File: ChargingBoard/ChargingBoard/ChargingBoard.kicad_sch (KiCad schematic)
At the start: 142 parts, among them J1 Conn_02x03_Odd_Even, J17 Micro_SD_Card, J2 Screw_Terminal_01x02, J3 Screw_Terminal_01x02, J4 Screw_Terminal_01x02, J5 Screw_Terminal_01x02, Q1 FQP27P06, Q10 FQP27P06, Q11 FQP27P06, Q12 IRLZ44N, Q13 FQP27P06, Q14 FQP27P06, Q15 FQP27P06, Q16 IRLZ44N, Q2 FQP27P06, Q3 FQP27P06, Q4 IRLZ44N, Q5 FQP27P06, Q6 FQP27P06, Q7 FQP27P06, Q8 IRLZ44N, Q9 FQP27P06, U1 LTC4011CFE, U2 LTC4011CFE, U3 LP2985-3.3, U4 LTC4011CFE, U5 LTC4011CFE, U6 ATmega328P-A, U9 CD4050BPWR, Y1 16MHz

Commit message: Voltage Sensors Added
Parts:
- added C24: 0.1u, Capacitor_SMD:C_0603_1608Metric_Pad1.08x0.95mm_HandSolder, symbol Device:C
- added U7, U8: INA260, Package_SO:TSSOP-16_4.4x5mm_P0.65mm, symbol Sensor:INA260
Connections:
- net +5V: now also U7.10 (VS), U7.5 (A0), U8.10 (VS)
- net GND: now also C24.2, U7.11 (GND), U7.4 (A1), U7.6 (GND), U8.11 (GND), U8.4 (A1), U8.5 (A0), U8.6 (GND)
- net SD_CS: now also U6.14 (PB2); no longer U6.27 (PC4)
- net at U6.20 (AREF): now also C24.1
- net SCL: now reaches U6.28 (PC5)
- net SCL: now also U7.9 (SCL), U8.9 (SCL)
- new net: U7.1 (IN+), U7.12 (VBUS), U7.2 (IN+), U7.3 (IN+)
- new net: U8.1 (IN+), U8.12 (VBUS), U8.2 (IN+), U8.3 (IN+)
- new net Motor_Load: U8.14 (IN-), U8.15 (IN-), U8.16 (IN-)
- new net PCB_Load: U7.14 (IN-), U7.15 (IN-), U7.16 (IN-)
- new net SDA: U6.27 (PC4), U7.8 (SDA), U8.8 (SDA)
- no-connect marks 5 -> 21
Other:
- note added: "Motor Battery V/A Sensor"
- note added: "PCB Battery V/A Sensor"

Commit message: Fixed Power Flags
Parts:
- added J6: Conn_01x03_Pin, symbol Connector:Conn_01x03_Pin
- added J7: Screw_Terminal_01x02, symbol Connector:Screw_Terminal_01x02
- U3: footprint Package_TO_SOT_SMD:SOT-23-5_HandSoldering -> Package_TO_SOT_SMD:SOT-23-5
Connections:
- net DCIN1 is gone; now on net +34V_DCIN: J2.1 (Pin_1), J3.1 (Pin_1)
- net DCIN2 is gone; now on net +18V_DCIN: J4.1 (Pin_1)
- net BAT1: no longer R48.1, U5.12 (BAT)
- net BAT4: now also R48.1, U5.12 (BAT)
- net GND: now also J6.1 (Pin_1), J7.2 (Pin_2)
- net RX: now also J6.3 (Pin_3)
- net TX: now also J6.2 (Pin_2)
- net +18V_VCC: now reaches U7.1 (IN+), U7.12 (VBUS), U7.2 (IN+), U7.3 (IN+)
- net +18V_VCC: now also C15.1, C20.1, D15.1 (K), D20.1 (K), Q10.3 (S), Q11.3 (S), Q13.3 (S), Q14.3 (S), Q15.3 (S), Q9.3 (S), U4.18 (V_{CC}), U5.18 (V_{CC})
- net at J17.3 (CMD), U9.4: no longer J17.5 (CLK), U9.2
- net +12V renamed +34V_VCC
- net +34V_VCC: now also C10.1, C5.1, D10.1 (K), D5.1 (K), Q1.3 (S), Q2.3 (S), Q3.3 (S), Q6.3 (S), Q7.3 (S), U1.18 (V_{CC}), U2.18 (V_{CC}); no longer Q13.3 (S)
- net +18V renamed +18V_DCIN
- net +18V_DCIN: now also J7.1 (Pin_1); no longer C15.1, C20.1, D15.1 (K), D20.1 (K), Q10.3 (S), Q11.3 (S), Q14.3 (S), Q15.3 (S), Q9.3 (S), U4.18 (V_{CC}), U5.18 (V_{CC})
- net +34V renamed +34V_DCIN
- net +34V_DCIN: no longer C10.1, C5.1, D10.1 (K), D5.1 (K), Q1.3 (S), Q2.3 (S), Q3.3 (S), Q6.3 (S), Q7.3 (S), U1.18 (V_{CC}), U2.18 (V_{CC})
- new net: J17.5 (CLK), U9.2
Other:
- moved on the sheet: C22, C23, J5, U3, U7, U8

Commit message: Component Reworks
Changed MOSFET component footprints, diodes, etc.
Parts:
- removed C14, C19, C4, C9: 10u, Capacitor_SMD:C_0201_0603Metric_Pad0.64x0.40mm_HandSolder, symbol Device:C
- removed Q10, Q11, Q13, Q14, Q15, Q9: FQP27P06, Package_TO_SOT_THT:TO-220-3_Vertical, symbol Transistor_FET:FQP27P06
- added C14, C19, C4, C9: 10u, Capacitor_THT:CP_Radial_D5.0mm_P2.00mm, symbol Device:C_Polarized
- added Q10, Q9: FDC658AP, Package_TO_SOT_SMD:SuperSOT-6, symbol FDC658AP:FDC658AP
- added U10, U11: FDS6975, Package_SO:SOIC-8_3.9x4.9mm_P1.27mm, symbol FDS6975:FDS6975
- BT1, BT2, BT3, BT4: footprint Battery:BatteryHolder_Keystone_1060_1x2032 -> TerminalBlock_Phoenix:TerminalBlock_Phoenix_MKDS-1,5-2-5.08_1x02_P5.08mm_Horizontal
- C1, C11, C12, C13, C16, C17, C18, C2, C3, C6, C7, C8: footprint Capacitor_SMD:C_0201_0603Metric_Pad0.64x0.40mm_HandSolder -> Capacitor_SMD:C_0603_1608Metric_Pad1.08x0.95mm_HandSolder
- C10, C15, C20, C5: footprint (none) -> Capacitor_THT:CP_Radial_D5.0mm_P2.00mm
- D1, D11, D12, D13, D14, D16, D17, D18, D19, D2, D3, D4, D6, D7, D8, D9: footprint LED_SMD:LED_0201_0603Metric_Pad0.64x0.40mm_HandSolder -> LED_SMD:LED_0603_1608Metric_Pad1.05x0.95mm_HandSolder
- D10, D15, D20, D5: footprint Diode_THT:D_DO-41_SOD81_P10.16mm_Horizontal -> Diode_SMD:D_SMA-SMB_Universal_Handsoldering
- J1: footprint (none) -> Connector_PinSocket_2.54mm:PinSocket_2x03_P2.54mm_Vertical
- J2, J3, J4, J5, J7: footprint (none) -> TerminalBlock_Phoenix:TerminalBlock_Phoenix_MKDS-1,5-2-5.08_1x02_P5.08mm_Horizontal
- J6: footprint (none) -> Connector_PinHeader_2.54mm:PinHeader_1x03_P2.54mm_Vertical
- L1, L2, L3, L4: value 6.8u -> 10u; footprint Inductor_SMD:L_0201_0603Metric_Pad0.64x0.40mm_HandSolder -> Inductor_SMD:L_0603_1608Metric_Pad1.05x0.95mm_HandSolder
- Q1, Q12, Q16, Q2, Q3, Q4, Q5, Q6, Q7, Q8: footprint Package_TO_SOT_THT:TO-220-3_Vertical -> Package_TO_SOT_SMD:TO-252-2
- R1, R10, R11, R12, R13, R14, R15, R16, R17, R18, R19, R2, R20, R21, R22, R23, R24, R25, R26, R27, R28, R29, R3, R30, R31, R32, R33, R34, R35, R36, R37, R38, R39, R4, R40, R41, R42, R43, R44, R45, R46, R47, R48, R49, R5, R50, R51, R52, R6, R7, R8, R9: footprint Resistor_SMD:R_0201_0603Metric_Pad0.64x0.40mm_HandSolder -> Resistor_SMD:R_0603_1608Metric_Pad0.98x0.95mm_HandSolder
- R54, R55, R56: footprint (none) -> Resistor_SMD:R_0603_1608Metric_Pad0.98x0.95mm_HandSolder
- TH1, TH2, TH3, TH4: footprint Resistor_SMD:R_0508_1220Metric_Pad1.12x2.15mm_HandSolder -> Resistor_SMD:R_0603_1608Metric_Pad0.98x0.95mm_HandSolder
- Y1: footprint (none) -> Crystal:Resonator_Murata_DSN6-3Pin_W7.0mm_H2.5mm
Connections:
- net +18V_DCIN: now also U10.5 (D2), U10.6 (D2), U11.5 (D2), U11.6 (D2)
- net +18V_VCC: now also Q10.4 (S), Q9.4 (S), U10.1 (S1), U10.3 (S2), U11.1 (S1), U11.3 (S2)
- net +34V_VCC: now also U8.1 (IN+), U8.12 (VBUS), U8.2 (IN+), U8.3 (IN+)
- net BAT1: now also C4.1
- net BAT2: now also C9.1
- net BAT3: now also C14.1, U10.7 (D1), U10.8 (D1)
- net BAT4: now also C19.1, U11.7 (D1), U11.8 (D1)
- net GND: now also C14.2, C19.2, C4.2, C9.2
- net INFET3: now also U10.4 (G2)
- net INFET4: now also U11.4 (G2)
- net L3: now also Q10.1 (D), Q10.2 (D), Q10.5 (D), Q10.6 (D)
- net L4: now also Q9.1 (D), Q9.2 (D), Q9.5 (D), Q9.6 (D)
- net TGATE3: now also Q10.3 (G)
- net TGATE4: now also Q9.3 (G)
- net at D20.2 (A), R47.1: now also U11.2 (G1)
- net at D15.2 (A), R34.1: now also U10.2 (G1)
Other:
- moved on the sheet: C15, C20, C24, D15, D20, J1, Q12, Q16, R21, R34, R47

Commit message: Arrangement Begins
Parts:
- BT1, BT2, BT3, BT4: footprint TerminalBlock_Phoenix:TerminalBlock_Phoenix_MKDS-1,5-2-5.08_1x02_P5.08mm_Horizontal -> TerminalBlock_Phoenix:TerminalBlock_Phoenix_MPT-0,5-2-2.54_1x02_P2.54mm_Horizontal
- D10, D5: footprint Diode_SMD:D_SMA-SMB_Universal_Handsoldering -> Diode_SMD:D_SMA_Handsoldering
- D15, D20: footprint Diode_SMD:D_SMA-SMB_Universal_Handsoldering -> Diode_SMD:D_SOD-323_HandSoldering
- J2, J3, J4, J5, J7: footprint TerminalBlock_Phoenix:TerminalBlock_Phoenix_MKDS-1,5-2-5.08_1x02_P5.08mm_Horizontal -> TerminalBlock_Phoenix:TerminalBlock_Phoenix_MKDS-1-2-3.81_1x02_P3.81mm_Horizontal
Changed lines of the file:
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@@
 			)
 		)
-		(property "Footprint" "TerminalBlock_Phoenix:TerminalBlock_Phoenix_MKDS-1,5-2-5.08_1x02_P5.08mm_Horizontal"
+		(property "Footprint" "TerminalBlock_Phoenix:TerminalBlock_Phoenix_MPT-0,5-2-2.54_1x02_P2.54mm_Horizontal"
 			(at 525.78 168.656 90)
 			(effects
@@
 			)
 		)
-		(property "Footprint" "TerminalBlock_Phoenix:TerminalBlock_Phoenix_MKDS-1,5-2-5.08_1x02_P5.08mm_Horizontal"
+		(property "Footprint" "TerminalBlock_Phoenix:TerminalBlock_Phoenix_MKDS-1-2-3.81_1x02_P3.81mm_Horizontal"
 			(at 196.85 21.59 0)
 			(effects
@@
 			)
 		)
-		(property "Footprint" "TerminalBlock_Phoenix:TerminalBlock_Phoenix_MKDS-1,5-2-5.08_1x02_P5.08mm_Horizontal"
+		(property "Footprint" "TerminalBlock_Phoenix:TerminalBlock_Phoenix_MKDS-1-2-3.81_1x02_P3.81mm_Horizontal"
 			(at 196.85 59.69 0)
 			(effects
@@
 			)
 		)
-		(property "Footprint" "TerminalBlock_Phoenix:TerminalBlock_Phoenix_MKDS-1,5-2-5.08_1x02_P5.08mm_Horizontal"
+		(property "Footprint" "TerminalBlock_Phoenix:TerminalBlock_Phoenix_MKDS-1-2-3.81_1x02_P3.81mm_Horizontal"
 			(at 196.85 39.37 0)
 			(effects
@@
 			)
 		)
-		(property "Footprint" "Diode_SMD:D_SMA-SMB_Universal_Handsoldering"
+		(property "Footprint" "Diode_SMD:D_SOD-323_HandSoldering"
 			(at 480.695 115.57 0)
 			(effects
@@
 			)
 		)
-		(property "Footprint" "TerminalBlock_Phoenix:TerminalBlock_Phoenix_MKDS-1,5-2-5.08_1x02_P5.08mm_Horizontal"
+		(property "Footprint" "TerminalBlock_Phoenix:TerminalBlock_Phoenix_MPT-0,5-2-2.54_1x02_P2.54mm_Horizontal"
 			(at 370.84 81.026 90)
 			(effects
@@
 			)
 		)
-		(property "Footprint" "Diode_SMD:D_SMA-SMB_Universal_Handsoldering"
+		(property "Footprint" "Diode_SMD:D_SOD-323_HandSoldering"
 			(at 323.215 114.3 0)
 			(effects
@@
 			)
 		)
-		(property "Footprint" "TerminalBlock_Phoenix:TerminalBlock_Phoenix_MKDS-1,5-2-5.08_1x02_P5.08mm_Horizontal"
+		(property "Footprint" "TerminalBlock_Phoenix:TerminalBlock_Phoenix_MPT-0,5-2-2.54_1x02_P2.54mm_Horizontal"
 			(at 370.84 168.656 90)
 			(effects
@@
 			)
 		)
-		(property "Footprint" "TerminalBlock_Phoenix:TerminalBlock_Phoenix_MKDS-1,5-2-5.08_1x02_P5.08mm_Horizontal"
+		(property "Footprint" "TerminalBlock_Phoenix:TerminalBlock_Phoenix_MKDS-1-2-3.81_1x02_P3.81mm_Horizontal"
 			(at 196.85 30.48 0)
 			(effects
@@
 			)
 		)
-		(property "Footprint" "TerminalBlock_Phoenix:TerminalBlock_Phoenix_MKDS-1,5-2-5.08_1x02_P5.08mm_Horizontal"
+		(property "Footprint" "TerminalBlock_Phoenix:TerminalBlock_Phoenix_MPT-0,5-2-2.54_1x02_P2.54mm_Horizontal"
 			(at 525.78 81.026 90)
 			(effects
@@
 			)
 		)
-		(property "Footprint" "TerminalBlock_Phoenix:TerminalBlock_Phoenix_MKDS-1,5-2-5.08_1x02_P5.08mm_Horizontal"
+		(property "Footprint" "TerminalBlock_Phoenix:TerminalBlock_Phoenix_MKDS-1-2-3.81_1x02_P3.81mm_Horizontal"
 			(at 196.85 49.53 0)
 			(effects
@@
 			)
 		)
-		(property "Footprint" "Diode_SMD:D_SMA-SMB_Universal_Handsoldering"
+		(property "Footprint" "Diode_SMD:D_SMA_Handsoldering"
 			(at 478.155 29.21 0)
 			(effects
@@
 			)
 		)
-		(property "Footprint" "Diode_SMD:D_SMA-SMB_Universal_Handsoldering"
+		(property "Footprint" "Diode_SMD:D_SMA_Handsoldering"
 			(at 323.215 29.21 0)
 			(effects

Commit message: More Arranging
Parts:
- R13, R23, R36, R49: footprint Resistor_SMD:R_0603_1608Metric_Pad0.98x0.95mm_HandSolder -> Resistor_SMD:R_0805_2012Metric_Pad1.20x1.40mm_HandSolder
- renumbered J7 to J5, J5 to J7
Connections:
- net +18V_DCIN: now also U10.7 (D1), U10.8 (D1), U11.7 (D1), U11.8 (D1); no longer U10.5 (D2), U10.6 (D2), U11.5 (D2), U11.6 (D2)
- net BAT3: now also U10.5 (D2), U10.6 (D2); no longer U10.7 (D1), U10.8 (D1)
- net BAT4: now also U11.5 (D2), U11.6 (D2); no longer U11.7 (D1), U11.8 (D1)
- net INFET3: now also U10.2 (G1); no longer U10.4 (G2)
- net INFET4: now also U11.2 (G1); no longer U11.4 (G2)
- net at D20.2 (A), R47.1: now also U11.4 (G2); no longer U11.2 (G1)
- net at D15.2 (A), R34.1: now also U10.4 (G2); no longer U10.2 (G1)
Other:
- moved on the sheet: C15, C20, D15, D20, R34, R47, U10, U11

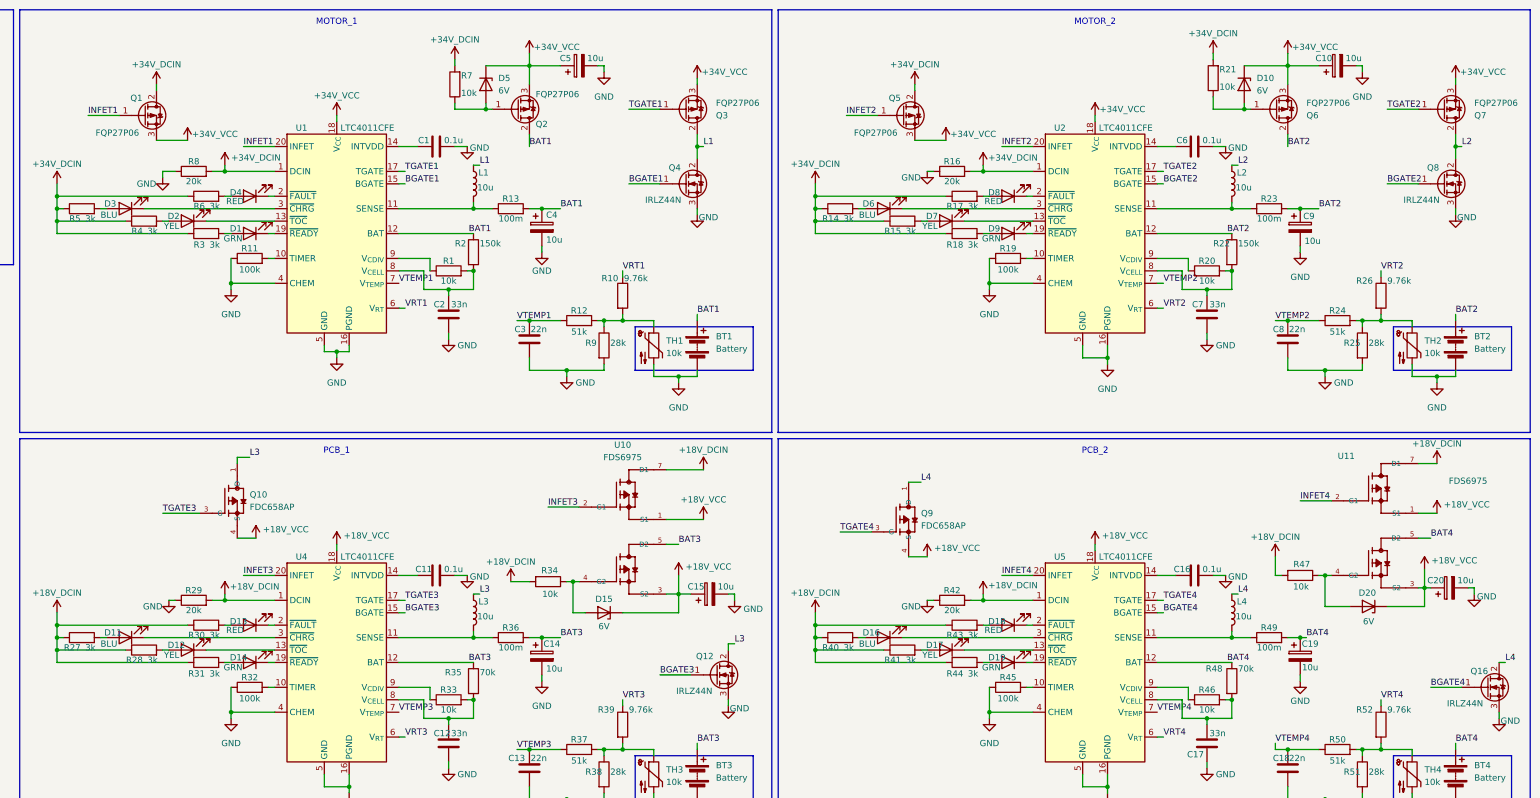
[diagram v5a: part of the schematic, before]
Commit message: MOSFETs changed
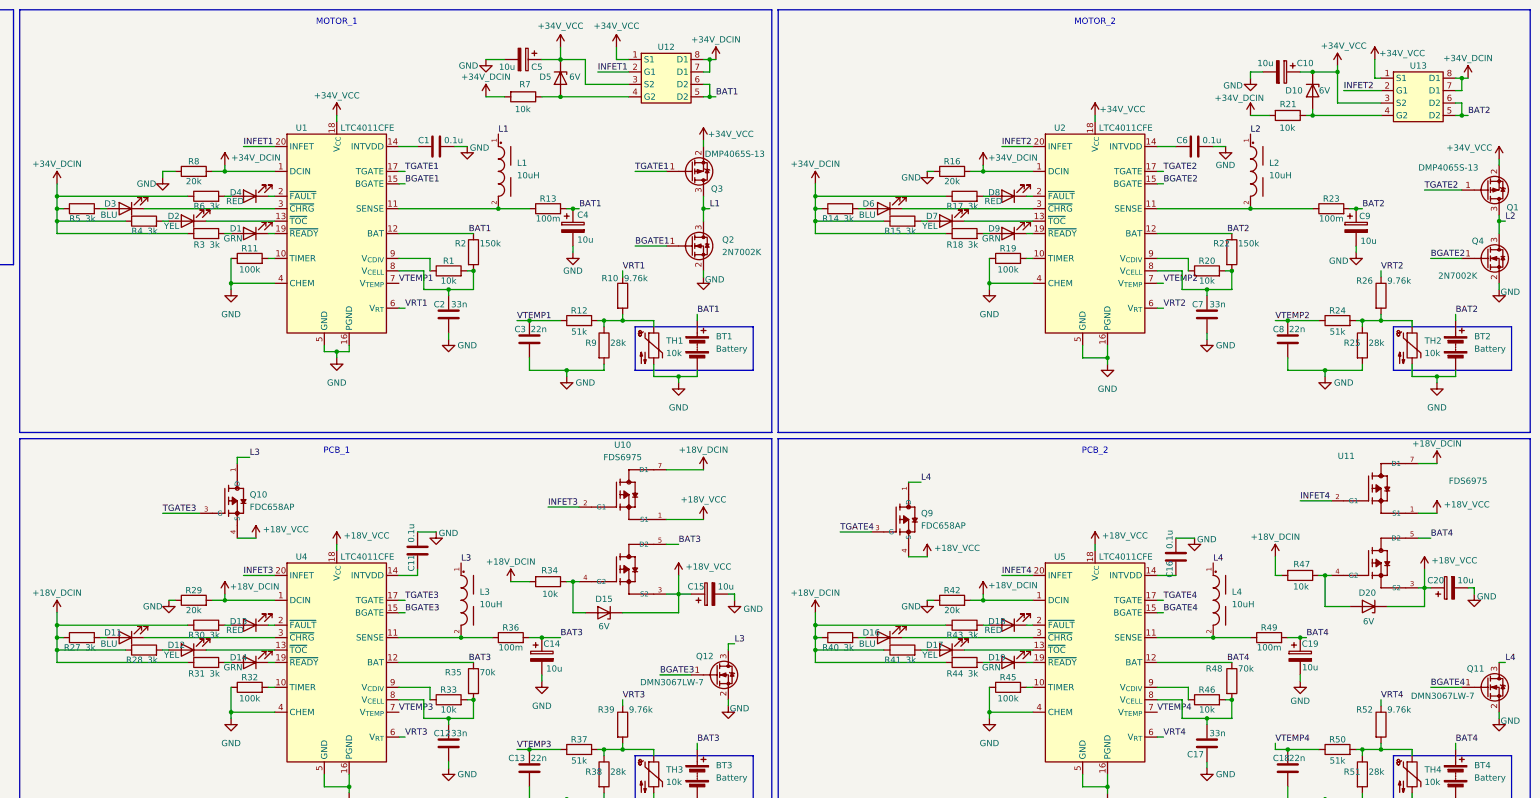
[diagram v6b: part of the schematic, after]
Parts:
- removed L1, L2, L3, L4: 10u, Inductor_SMD:L_0603_1608Metric_Pad1.05x0.95mm_HandSolder, symbol Device:L
- removed Q16, Q4, Q8: IRLZ44N, Package_TO_SOT_SMD:TO-252-2, symbol Transistor_FET:IRLZ44N
- removed Q2, Q5, Q6, Q7: FQP27P06, Package_TO_SOT_SMD:TO-252-2, symbol Transistor_FET:FQP27P06
- added L1, L2, L3, L4: 10uH, WE-LHMI_7050:WE-LHMI_7050, symbol WE-LHMI_7050:WE-LHMI_7050
- added Q11: DMN3067LW-7, Package_TO_SOT_SMD:SOT-323_SC-70, symbol Transistor_FET:IRLZ44N
- added Q2, Q4: 2N7002K, Package_TO_SOT_SMD:SOT-23, symbol Transistor_FET:2N7002K
- added U12, U13: Si4909DY-T1-GE3, Package_SO:SOIC-8_3.9x4.9mm_P1.27mm, symbol ChargingBoard:Si4909DY-T1-GE3
- D10, D5: footprint Diode_SMD:D_SMA_Handsoldering -> Diode_SMD:D_SOD-123F
- Q1, Q3: value FQP27P06 -> DMP4065S-13; footprint Package_TO_SOT_SMD:TO-252-2 -> Package_TO_SOT_SMD:SOT-23
- Q12: value IRLZ44N -> DMN3067LW-7; footprint Package_TO_SOT_SMD:TO-252-2 -> Package_TO_SOT_SMD:SOT-323_SC-70
- TH1, TH2, TH3, TH4: footprint Resistor_SMD:R_0603_1608Metric_Pad0.98x0.95mm_HandSolder -> Connector_PinHeader_2.54mm:PinHeader_1x02_P2.54mm_Vertical
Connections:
- net +34V_DCIN: now also U12.7 (D1), U12.8 (D1), U13.7 (D1), U13.8 (D1); no longer Q1.2 (D)
- net +34V_VCC: now also Q1.2 (S), Q3.2 (S), U12.1 (S1), U12.3 (S2), U13.1 (S1), U13.3 (S2); no longer Q1.3 (S), Q3.3 (S)
- net BAT1: now also U12.5 (D2), U12.6 (D2)
- net BAT2: now also U13.5 (D2), U13.6 (D2)
- net BGATE1: now also Q2.1 (G)
- net BGATE2: now also Q4.1 (G)
- net BGATE4: now also Q11.1 (G)
- net GND: now also Q12.2 (S), Q11.2 (S), Q2.2 (S), Q4.2 (S); no longer Q12.3 (S)
- net INFET1: now also U12.2 (G1); no longer Q1.1 (G)
- net INFET2: now also U13.2 (G1)
- net L1: now also Q3.3 (D), L1.1, Q2.3 (D); no longer Q3.2 (D)
- net L2: now also Q1.3 (D), L2.1, Q4.3 (D)
- net L3: now also Q12.3 (D), L3.1; no longer Q12.2 (D)
- net L4: now also L4.1, Q11.3 (D)
- net TGATE2: now also Q1.1 (G)
- net at D10.2 (A), R21.1: now also U13.4 (G2)
- net at R36.1, U4.11 (SENSE): now also L3.2
- net at R13.1, U1.11 (SENSE): now also L1.2
- net at R49.1, U5.11 (SENSE): now also L4.2
- net at D5.2 (A), R7.1: now also U12.4 (G2)
- net at R23.1, U2.11 (SENSE): now also L2.2
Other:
- moved on the sheet: C10, C11, C16, C4, C5, C9, D10, D5, Q3, R13, R21, R23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

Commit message: Board Done
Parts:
- added J8, J9: Screw_Terminal_01x02, TerminalBlock_Phoenix:TerminalBlock_Phoenix_MKDS-1-2-3.81_1x02_P3.81mm_Horizontal, symbol Connector:Screw_Terminal_01x02
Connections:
- net GND: now also J8.1 (Pin_1), J9.1 (Pin_1)
- net Motor_Load: now also J8.2 (Pin_2)
- net PCB_Load: now also J9.2 (Pin_2)

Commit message: Finishing Touches
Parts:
- removed J2: Screw_Terminal_01x02, TerminalBlock_Phoenix:TerminalBlock_Phoenix_MKDS-1-2-3.81_1x02_P3.81mm_Horizontal, symbol Connector:Screw_Terminal_01x02
- added C25: 10uF, Capacitor_THT:CP_Axial_L10.0mm_D4.5mm_P15.00mm_Horizontal, symbol Device:C_Polarized
- added J10: Barrel_Jack_MountingPin, Connector_BarrelJack:BarrelJack_GCT_DCJ200-10-A_Horizontal, symbol Connector:Barrel_Jack_MountingPin
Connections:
- net +34V_DCIN: now also C25.1, J10.1
- net GND: now also C25.2, J10.2
- no-connect marks 21 -> 22
